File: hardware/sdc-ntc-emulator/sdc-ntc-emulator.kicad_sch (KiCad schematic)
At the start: 33 parts, among them J1 DevKit J1, J2 DevKit J3, J3 5V IN (RAC03), J4 SDC VE1 / GND, K1 G5V-2-H1 5VDC, Q1 AO3400A, U1 ISO1540, U2 AD5272BRMZ-50

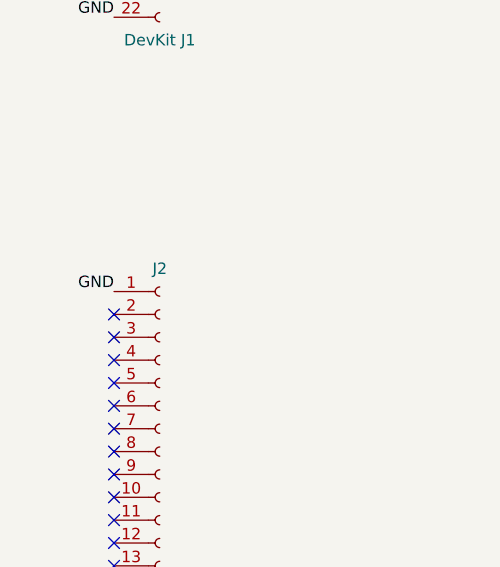
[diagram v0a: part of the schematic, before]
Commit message: PCB: fit the actual DevKit clone, fix antenna keep-out and GND split
The clone is shorter than the official DevKitC-1 and its module antenna
overhangs the DevKit edge right after pin 1, so the no-copper area now
starts there. That cut the ESP ground pour in two; an explicit GND track
from DevKit J1.22 to the TEM input ground reconnects it. Header row
spacing is now one constant (DEVKIT_ROWS, still 25.4 mm pending a
re-measurement).

Co-Authored-By: Claude Opus 5.5 <noreply@anthropic.com>
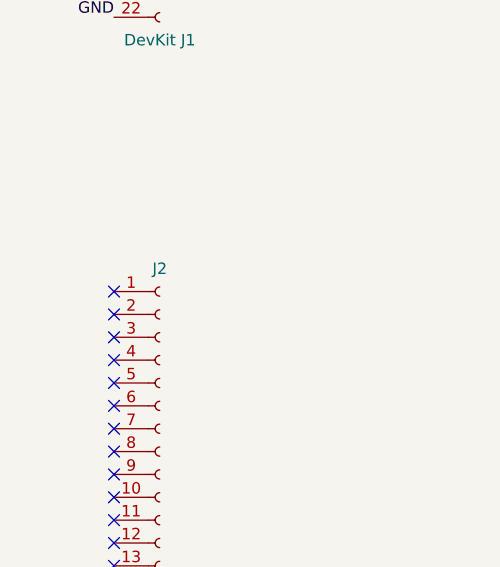
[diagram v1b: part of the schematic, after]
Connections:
- net GND: no longer J2.1 (Pin_1)
- no-connect marks 34 -> 35
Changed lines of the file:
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@@
-		)
-	)
-	(label "GND"
-		(at 25.4 134.62 180)
-		(fields_autoplaced yes)
-		(effects
-			(font
-				(size 1.27 1.27)
-			)
-			(justify right bottom)
 		)
 	)
 	(no_connect
+		(at 25.4 134.62)
+	)
+	(no_connect

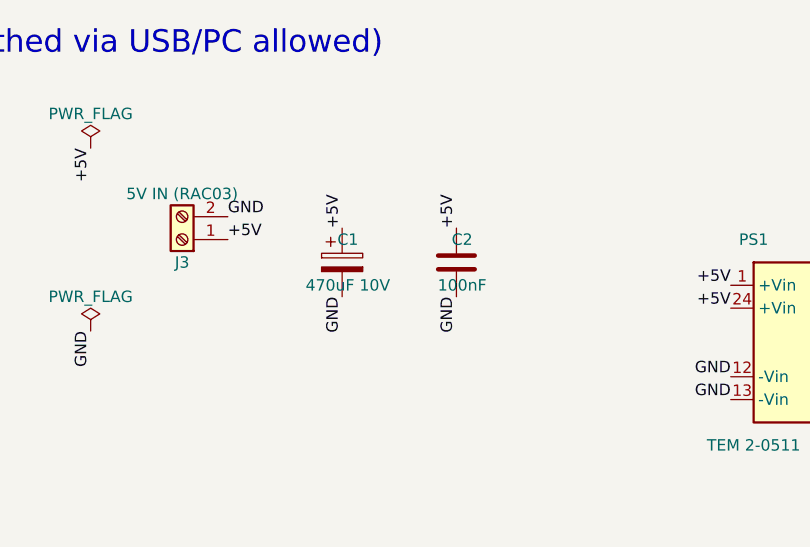
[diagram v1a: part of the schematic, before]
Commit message: PCB: add 10 uF ceramic (C9) parallel to the 5 V input elco
Co-Authored-By: Claude Opus 5.5 <noreply@anthropic.com>
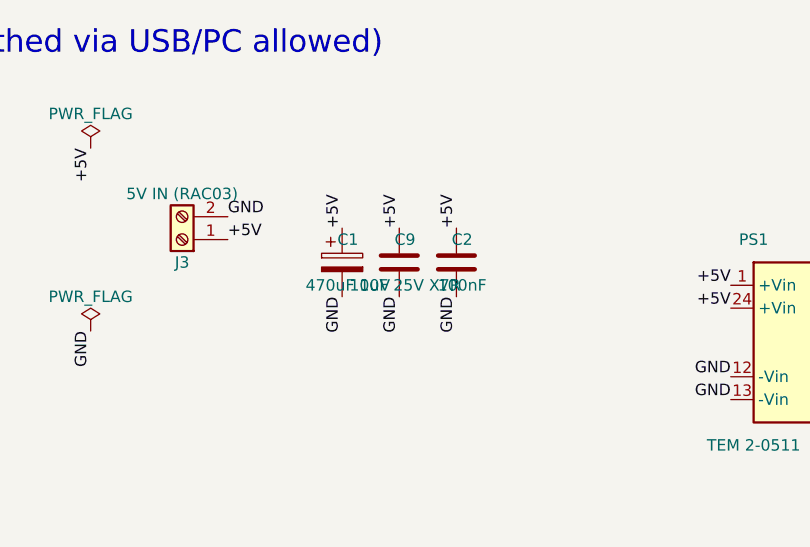
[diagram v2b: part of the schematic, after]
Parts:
- added C9: 10uF 25V X7R, Capacitor_SMD:C_1206_3216Metric_Pad1.33x1.80mm_HandSolder, symbol Device:C
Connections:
- net +5V: now also C9.1
- net GND: now also C9.2
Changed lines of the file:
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@@
+	(symbol
+		(lib_id "Device:C")
+		(at 95.25 38.1 0)
+		(unit 1)
+		(exclude_from_sim no)
+		(in_bom yes)
+		(on_board yes)
+		(dnp no)
+		(property "Reference" "C9"
+			(at 95.885 35.56 0)
+			(effects
+				(font
+					(size 1.27 1.27)
+				)
+			)
+		)
+		(property "Value" "10uF 25V X7R"
+			(at 95.885 40.64 0)
+			(effects
+				(font
+					(size 1.27 1.27)
+				)
+			)
+		)
+		(property "Footprint" "Capacitor_SMD:C_1206_3216Metric_Pad1.33x1.80mm_HandSolder"
+			(at 95.25 38.1 0)
+			(effects
+				(font
+					(size 1.27 1.27)
+				)
+				(hide yes)
+			)
+		)
+		(property "Datasheet" "~"
+			(at 95.25 38.1 0)
+			(effects
+				(font
+					(size 1.27 1.27)
+				)
+				(hide yes)
+			)
+		)
+		(property "Description" "Low-ESR ceramic parallel to C1: RAC03 ripple, fast Wi-Fi current edges"
+			(at 95.25 38.1 0)
+			(effects
+				(font
+					(size 1.27 1.27)
+				)
+				(hide yes)
+			)
+		)
+		(pin "1"
+		)
+		(pin "2"
+		)
+		(instances
+			(project "sdc-ntc-emulator"
+				(path "/d9cfafe7-d1f3-551b-a0cb-64d50125fa6c"
+					(reference "C9")
+					(unit 1)
+				)
+			)
+		)
+	)
+	(label "+5V"
+		(at 95.25 34.29 90)
+		(fields_autoplaced yes)
+		(effects
+			(font
+				(size 1.27 1.27)
+			)
+			(justify left bottom)
+		)
+	)
+	(label "GND"
+		(at 95.25 41.91 270)
+		(fields_autoplaced yes)
+		(effects
+			(font
+				(size 1.27 1.27)
+			)
+			(justify right bottom)
+		)
+	)
 	(symbol
 		(lib_id "Device:C")

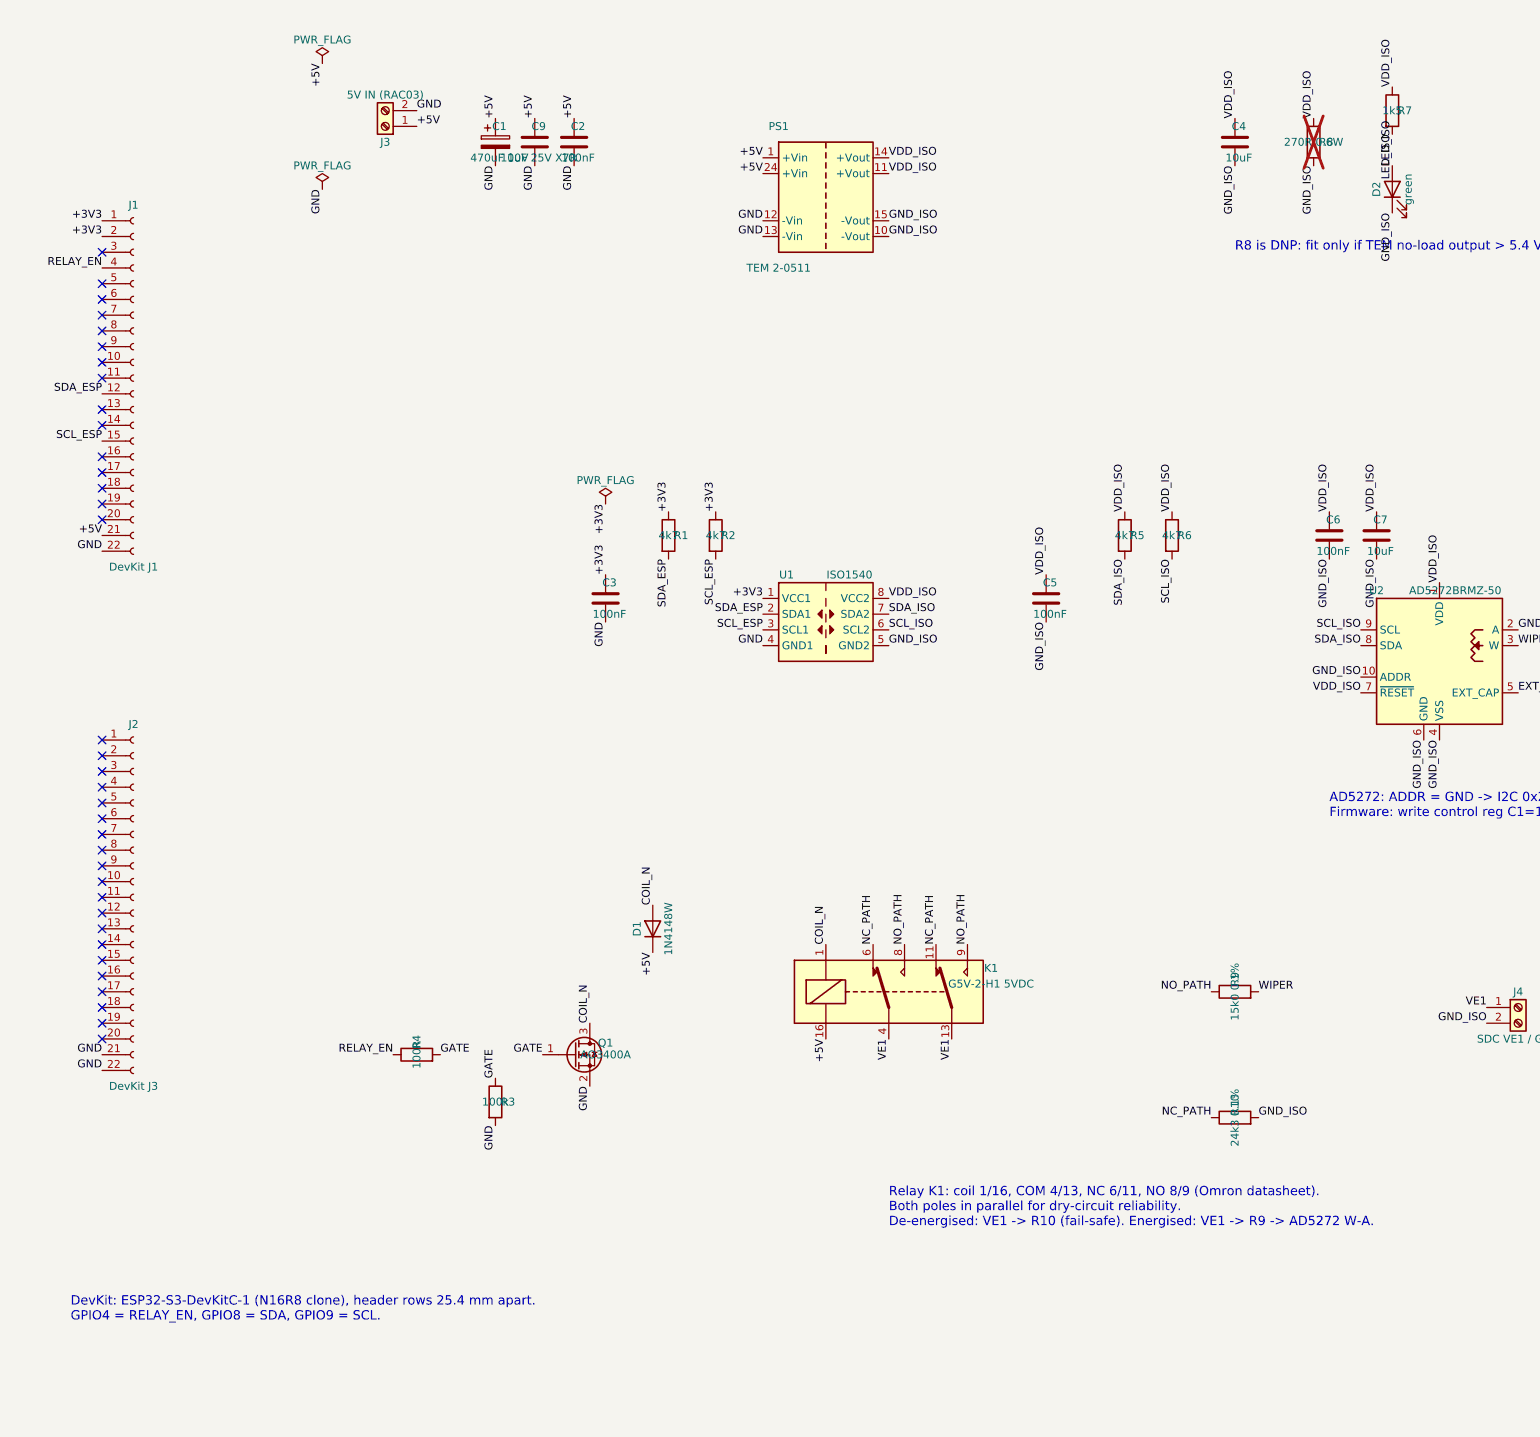
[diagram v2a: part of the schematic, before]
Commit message: PCB rev 2: apply the independent design review
- Isolation gap 0.40 -> 1.15 mm (oval TEM pads, wider domain outlines,
  router keeps full track width inside its domain); new
  tools/check_isolation.py measures the real copper gap and fails the build
  below 1.0 mm.
- Relay state sense (R11/R12 -> GPIO5) and reverse-polarity P-FET (Q2).
- R9 15.0k -> 18.2k (27 C floor if the AD5272 fails), R10 24.3k -> 24.9k
  (SDC +0.5 K offset), R1/R2 4.7k -> 2.7k (ISO1540 side-1 sink current).
- C3/C5 next to the ISO1540, relay holes 1.0 mm, AD5272 fan-out without
  wide tracks or vias under the chip, silkscreen >= 1.0 mm, X5-2..12 marking.
- Handoff/README: corrected X5-1, RAC03 limits, row spacing, LDO/preload
  leftovers; firmware requirements for readback, relay sense, ALWAYS_OFF.

Co-Authored-By: Claude Opus 5.5 <noreply@anthropic.com>
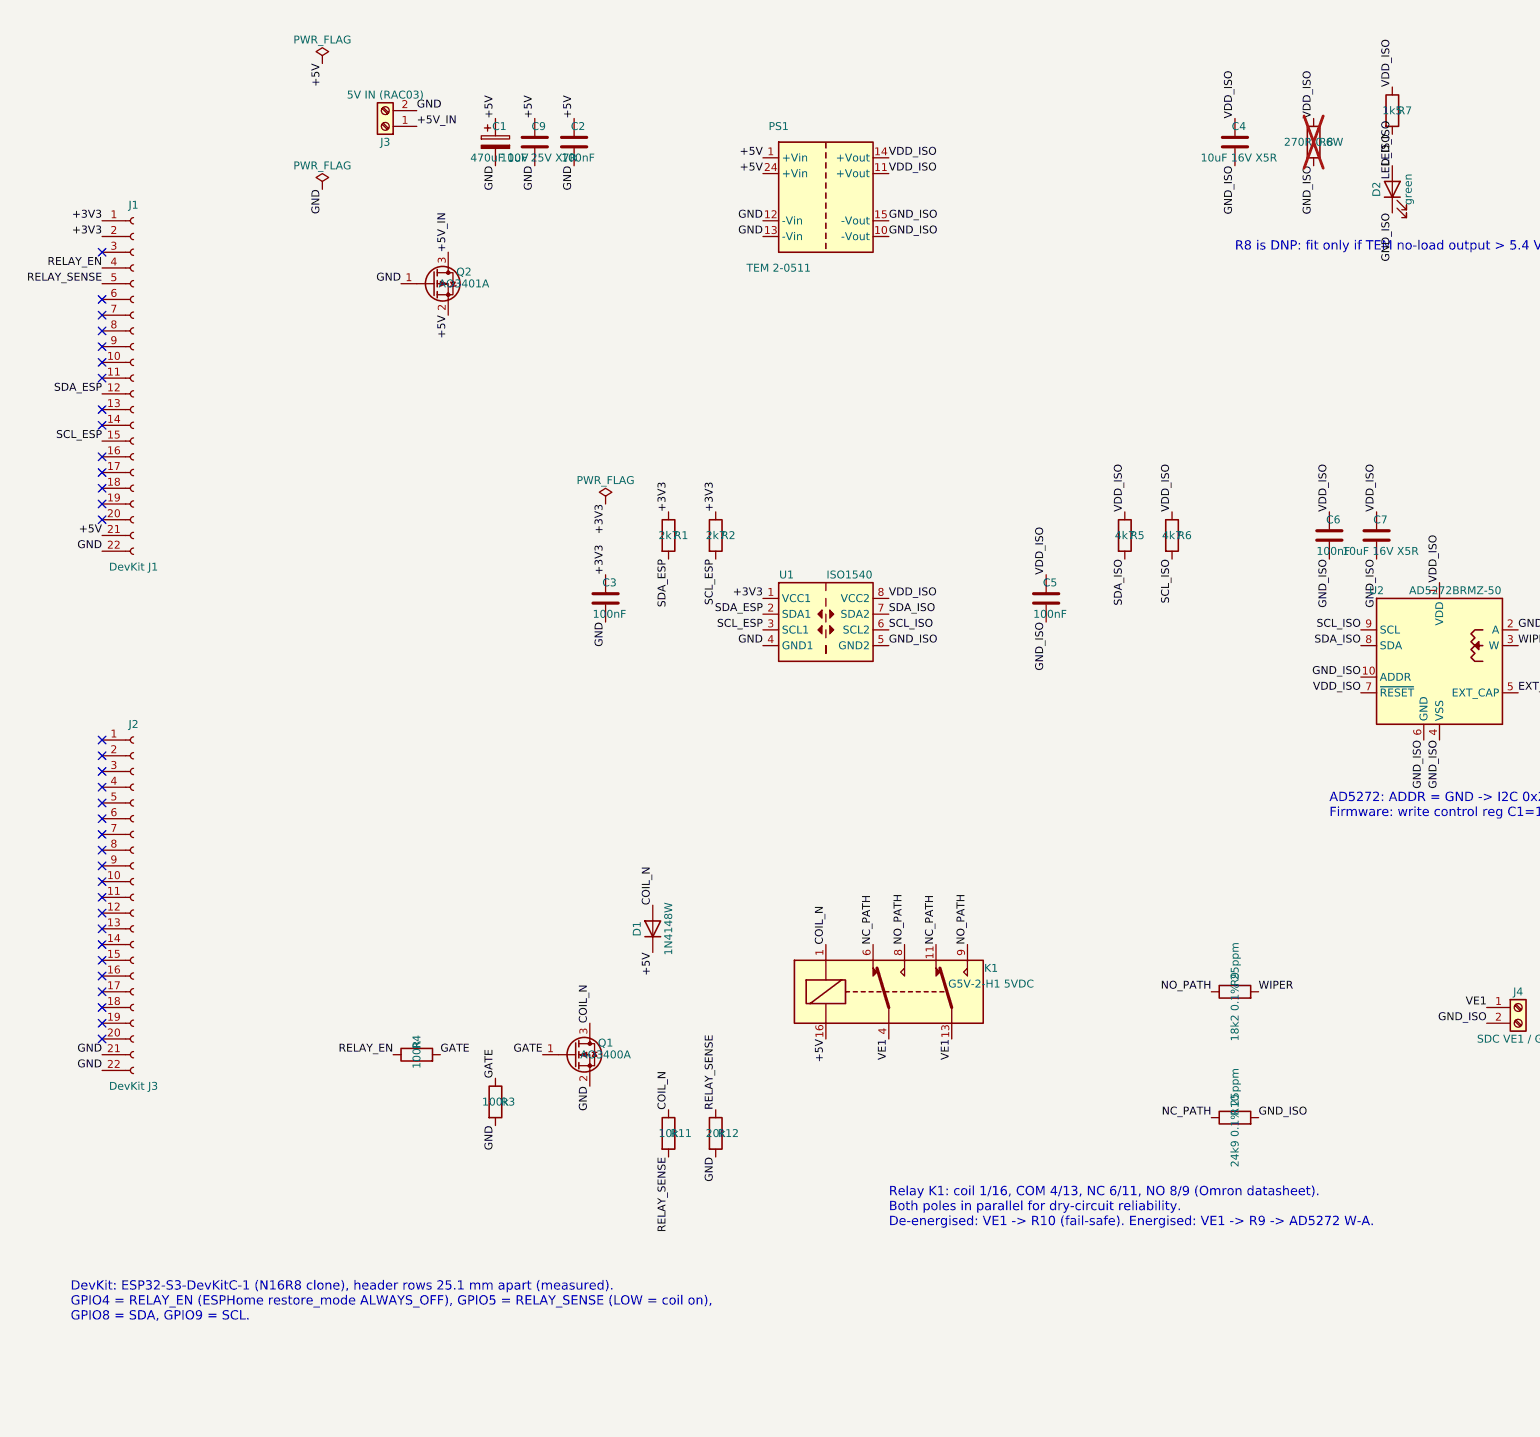
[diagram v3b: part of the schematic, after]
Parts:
- added Q2: AO3401A, Package_TO_SOT_SMD:SOT-23, symbol Transistor_FET:AO3401A
- added R11: 10k, Resistor_SMD:R_0805_2012Metric_Pad1.20x1.40mm_HandSolder, symbol Device:R
- added R12: 20k, Resistor_SMD:R_0805_2012Metric_Pad1.20x1.40mm_HandSolder, symbol Device:R
- C4, C7: value 10uF -> 10uF 16V X5R
- R1, R2: value 4k7 -> 2k7
- R10: value 24k3 0.1% -> 24k9 0.1% 25ppm
- R9: value 15k0 0.1% -> 18k2 0.1% 25ppm
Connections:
- net +5V: now also Q2.2 (S); no longer J3.1 (Pin_1)
- net COIL_N: now also R11.1
- net GND: now also Q2.1 (G), R12.2
- net RELAY_SENSE: now reaches J1.5 (Pin_5)
- net RELAY_SENSE: now also R11.2, R12.1
- new net +5V_IN: J3.1 (Pin_1), Q2.3 (D)
- no-connect marks 35 -> 34
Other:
- note added: "DevKit: ESP32-S3-DevKitC-1 (N16R8 clone), header rows 25.1 mm apart (measured). GPIO4 = RELAY_EN (ESPHome restore_mode ALWAYS_OFF), GPIO5 = RELAY_SENSE (LOW = coil on), GPIO8 = SDA, GPIO9 = SCL."
- note removed: "DevKit: ESP32-S3-DevKitC-1 (N16R8 clone), header rows 25.4 mm apart. GPIO4 = RELAY_EN, GPIO8 = SDA, GPIO9 = SCL."

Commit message: Add manufacturer part numbers and DigiKey BOM-Manager upload file
Co-Authored-By: Claude Opus 5.5 <noreply@anthropic.com>
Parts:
- C1: MPN (none) -> EEU-FR1A471; Manufacturer (none) -> Panasonic
- C2, C3, C5, C6: MPN (none) -> GRM21BR71H104KA01L; Manufacturer (none) -> Murata
- C4, C7: MPN (none) -> GRM21BR61C106KE15L; Manufacturer (none) -> Murata
- C8: MPN (none) -> GRM21BR71C105KA01L; Manufacturer (none) -> Murata
- C9: MPN (none) -> GRM31CR71E106KA12L; Manufacturer (none) -> Murata
- D1: MPN (none) -> 1N4148W-7-F; Manufacturer (none) -> Diodes Incorporated
- D2: MPN (none) -> LTST-C171GKT; Manufacturer (none) -> Lite-On
- J1, J2: MPN (none) -> PPTC221LFBN-RC; Manufacturer (none) -> Sullins Connector Solutions
- J3, J4: MPN (none) -> 1715721; Manufacturer (none) -> Phoenix Contact
- K1: MPN (none) -> G5V-2-H1 DC5; Manufacturer (none) -> Omron
- PS1: MPN (none) -> TEM 2-0511; Manufacturer (none) -> Traco Power
- Q1: MPN (none) -> AO3400A; Manufacturer (none) -> Alpha & Omega Semiconductor
- Q2: MPN (none) -> AO3401A; Manufacturer (none) -> Alpha & Omega Semiconductor
- R1, R2: MPN (none) -> RC0805FR-072K7L; Manufacturer (none) -> Yageo
- R10: MPN (none) -> RN55E2492BB14; Manufacturer (none) -> Vishay Dale
- R11: MPN (none) -> RC0805FR-0710KL; Manufacturer (none) -> Yageo
- R12: MPN (none) -> RC0805FR-0720KL; Manufacturer (none) -> Yageo
- R3: MPN (none) -> RC0805FR-07100KL; Manufacturer (none) -> Yageo
- R4: MPN (none) -> RC0805FR-07100RL; Manufacturer (none) -> Yageo
- R5, R6: MPN (none) -> RC0805FR-074K7L; Manufacturer (none) -> Yageo
- R7: MPN (none) -> RC0805FR-071K5L; Manufacturer (none) -> Yageo
- R8: MPN (none) -> MBB02070C2700FC100; Manufacturer (none) -> Vishay Beyschlag
- R9: MPN (none) -> RN55E1822BB14; Manufacturer (none) -> Vishay Dale
- U1: MPN (none) -> ISO1540DR; Manufacturer (none) -> Texas Instruments
- U2: MPN (none) -> AD5272BRMZ-50; Manufacturer (none) -> Analog Devices
